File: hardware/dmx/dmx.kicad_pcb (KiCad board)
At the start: 2 copper layers, 100 x 62 mm, 70 parts, among them J1 Midi In, J2 Midi Thru, J3 NeoPixel, J4 Power, J5 DMX, J6 I2C0, J7 I2C1, Q1 BSS138, Q2 BSS138, Q3 TSM680P06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

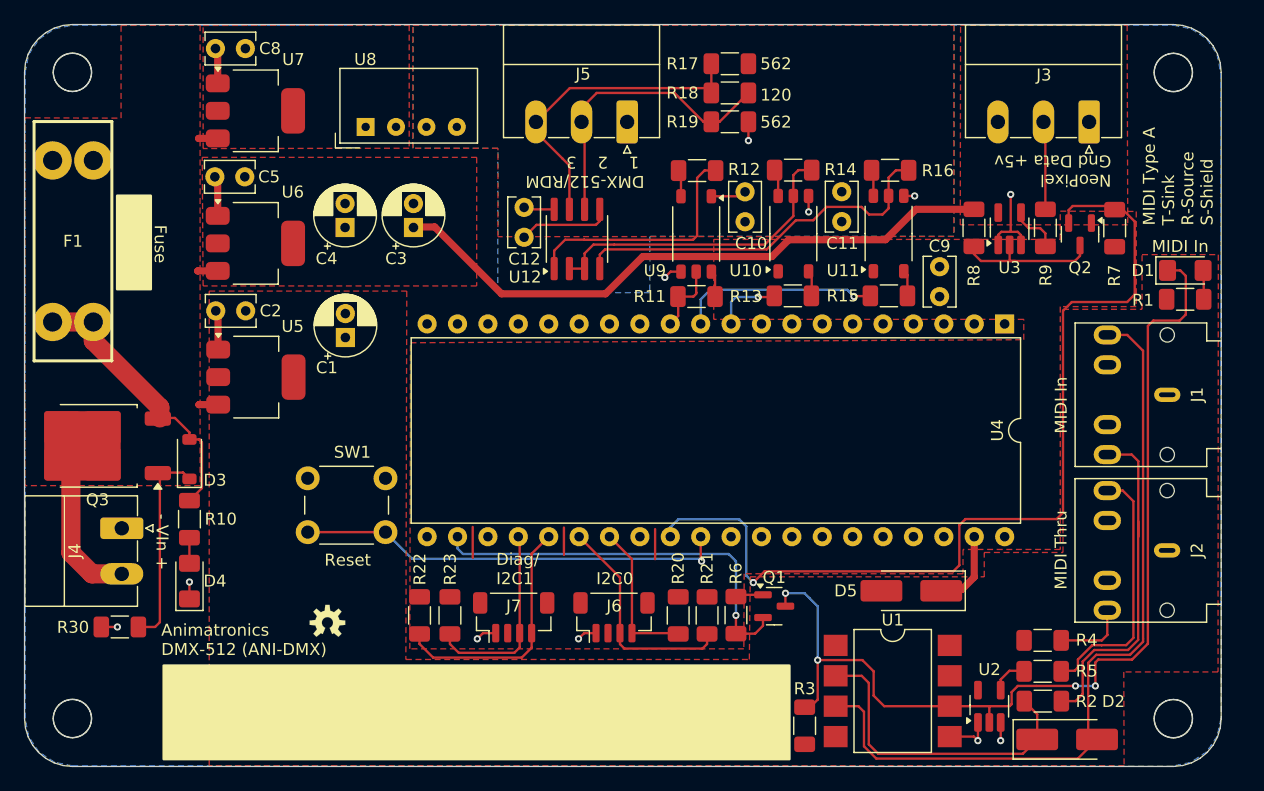
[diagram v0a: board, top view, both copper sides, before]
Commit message: Rev 1.1: - Update to latest KiCad - Fixed short in servo board - Updates to right-angle diag connector on servo boards - Fixed microproc footprint on diag board - Flipped I2C connector to top of diag board - Pass all ERC and DRC checks, add exclusions
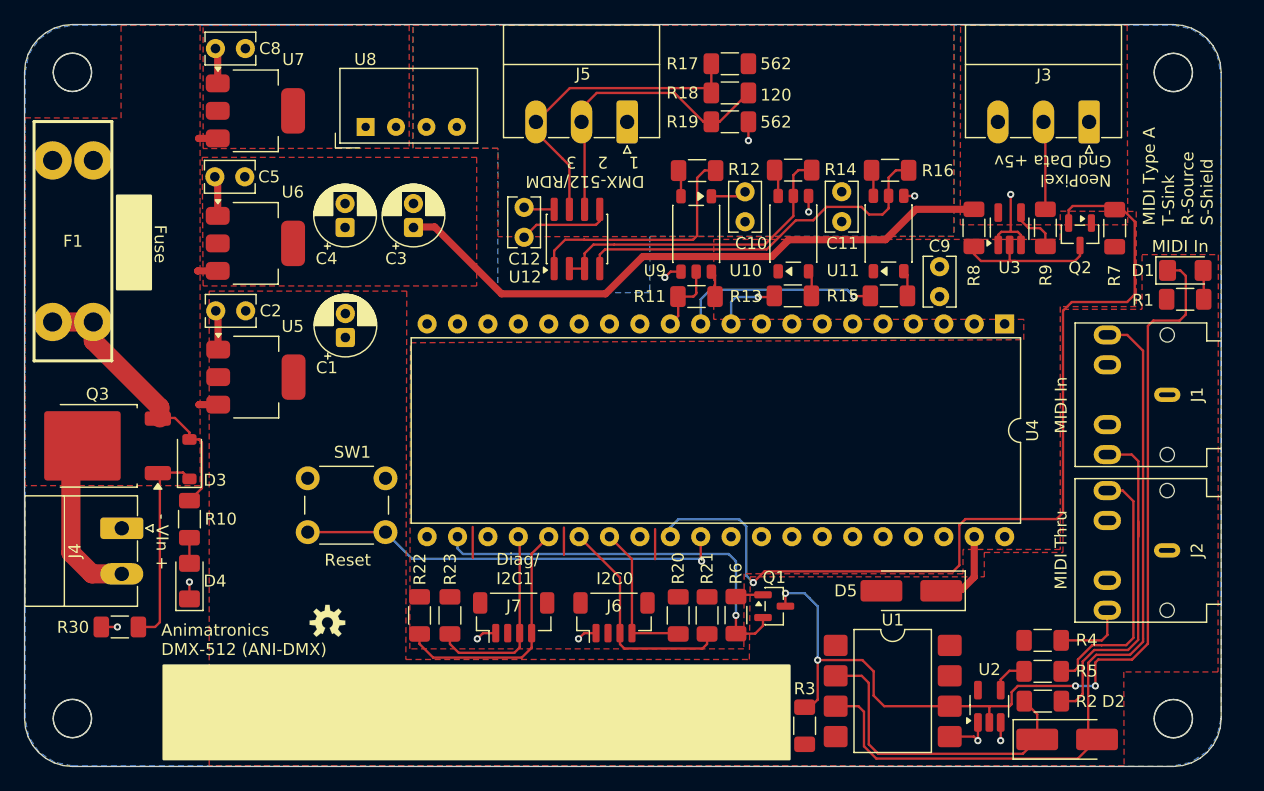
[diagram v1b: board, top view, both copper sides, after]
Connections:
- U4 pad 6: unconnected-(U4-GPIO4-Pad6) -> /~{DT-MBB}
- U4 pad 7: unconnected-(U4-GPIO5-Pad7) -> /~{DT-BRK}
- U4 pad 9: unconnected-(U4-GPIO6-Pad9) -> /~{DT-MAB}
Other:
- board text added: "ANI-DMX, Rev 1.1 Sparky Bobo Designs"
- board text removed: "ANI-DMX, Rev 1.0 Sparky Bobo Designs"
